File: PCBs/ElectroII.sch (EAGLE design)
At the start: 40 parts, among them J1 U.FL-R-SMT(01), T1 VIN, T2 VBAT, T3 GND, T4 BOOST, T5 VCC, T6 5V, U1 RFM95W-868S2, U2 TPS61090RSAR

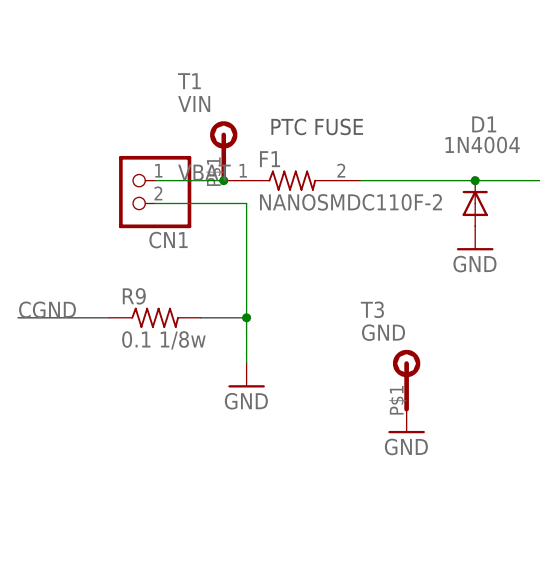
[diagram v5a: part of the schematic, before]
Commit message: Reviewed traces and fixed joints
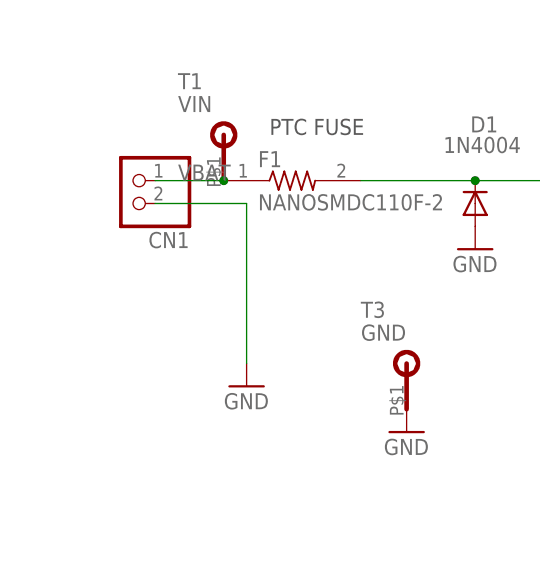
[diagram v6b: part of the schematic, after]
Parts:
- removed R9: 0.1 1/8w, RTR Main Library:R-ALL_PACKAGESR1206
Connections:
- removed net CGND: R9.1
- net GND: no longer R9.2
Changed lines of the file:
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@@
 <part name="P+9" library="RTR Main Library" deviceset="VCC" device=""/>
 <part name="P+10" library="RTR Main Library" deviceset="VCC" device=""/>
-<part name="R9" library="RTR Main Library" deviceset="R-ALL_PACKAGES" device="R1206" value="0.1 1/8w"/>
 <part name="D2" library="adafruit" library_urn="urn:adsk.eagle:library:420" deviceset="1N4004" device="" package3d_urn="urn:adsk.eagle:package:6240344/1"/>
 </parts>
@@
 <attribute name="VALUE" x="307.34" y="-53.34" size="1.778" layer="96" rot="R90"/>
 </instance>
-<instance part="R9" gate="G$1" x="27.94" y="-88.9" smashed="yes">
-<attribute name="NAME" x="24.13" y="-87.4014" size="1.778" layer="95"/>
-<attribute name="VALUE" x="24.13" y="-92.202" size="1.778" layer="96"/>
-</instance>
 <instance part="D2" gate="1" x="213.36" y="-73.66" smashed="yes">
 <attribute name="NAME" x="215.9" y="-73.1774" size="1.778" layer="95"/>
@@
 <wire x1="27.94" y1="-76.2" x2="38.1" y2="-76.2" width="0.1524" layer="91"/>
 <pinref part="GND25" gate="1" pin="GND"/>
-<wire x1="38.1" y1="-76.2" x2="38.1" y2="-88.9" width="0.1524" layer="91"/>
-<pinref part="R9" gate="G$1" pin="2"/>
-<wire x1="38.1" y1="-88.9" x2="38.1" y2="-93.98" width="0.1524" layer="91"/>
-<wire x1="33.02" y1="-88.9" x2="38.1" y2="-88.9" width="0.1524" layer="91"/>
-<junction x="38.1" y="-88.9"/>
+<wire x1="38.1" y1="-76.2" x2="38.1" y2="-93.98" width="0.1524" layer="91"/>
 </segment>
 <segment>
@@
 </segment>
 </net>
-<net name="CGND" class="0">
-<segment>
-<pinref part="R9" gate="G$1" pin="1"/>
-<wire x1="22.86" y1="-88.9" x2="12.7" y2="-88.9" width="0.1524" layer="91"/>
-<label x="12.7" y="-88.9" size="1.778" layer="95"/>
-</segment>
-</net>
